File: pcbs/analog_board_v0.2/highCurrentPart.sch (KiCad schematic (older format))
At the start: 29 parts, among them P2 CONN_01X03, P3 CONN_01X03, Q1 MMBT3904, U1 AD8616

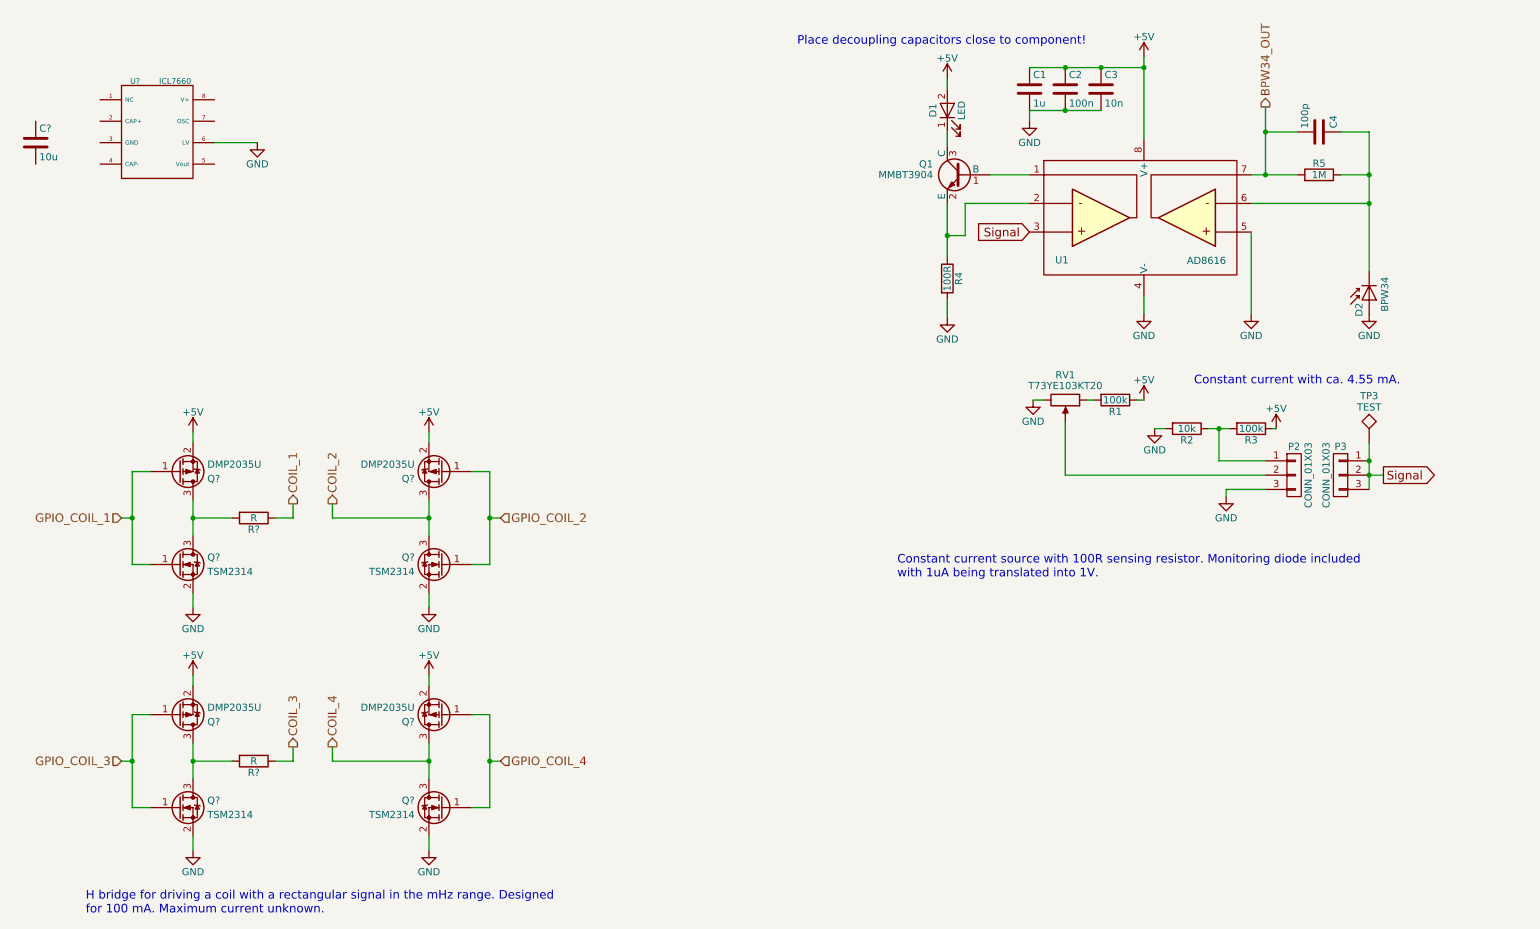
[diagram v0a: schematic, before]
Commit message: Finished schematics of the analog_board_v0.2 today.
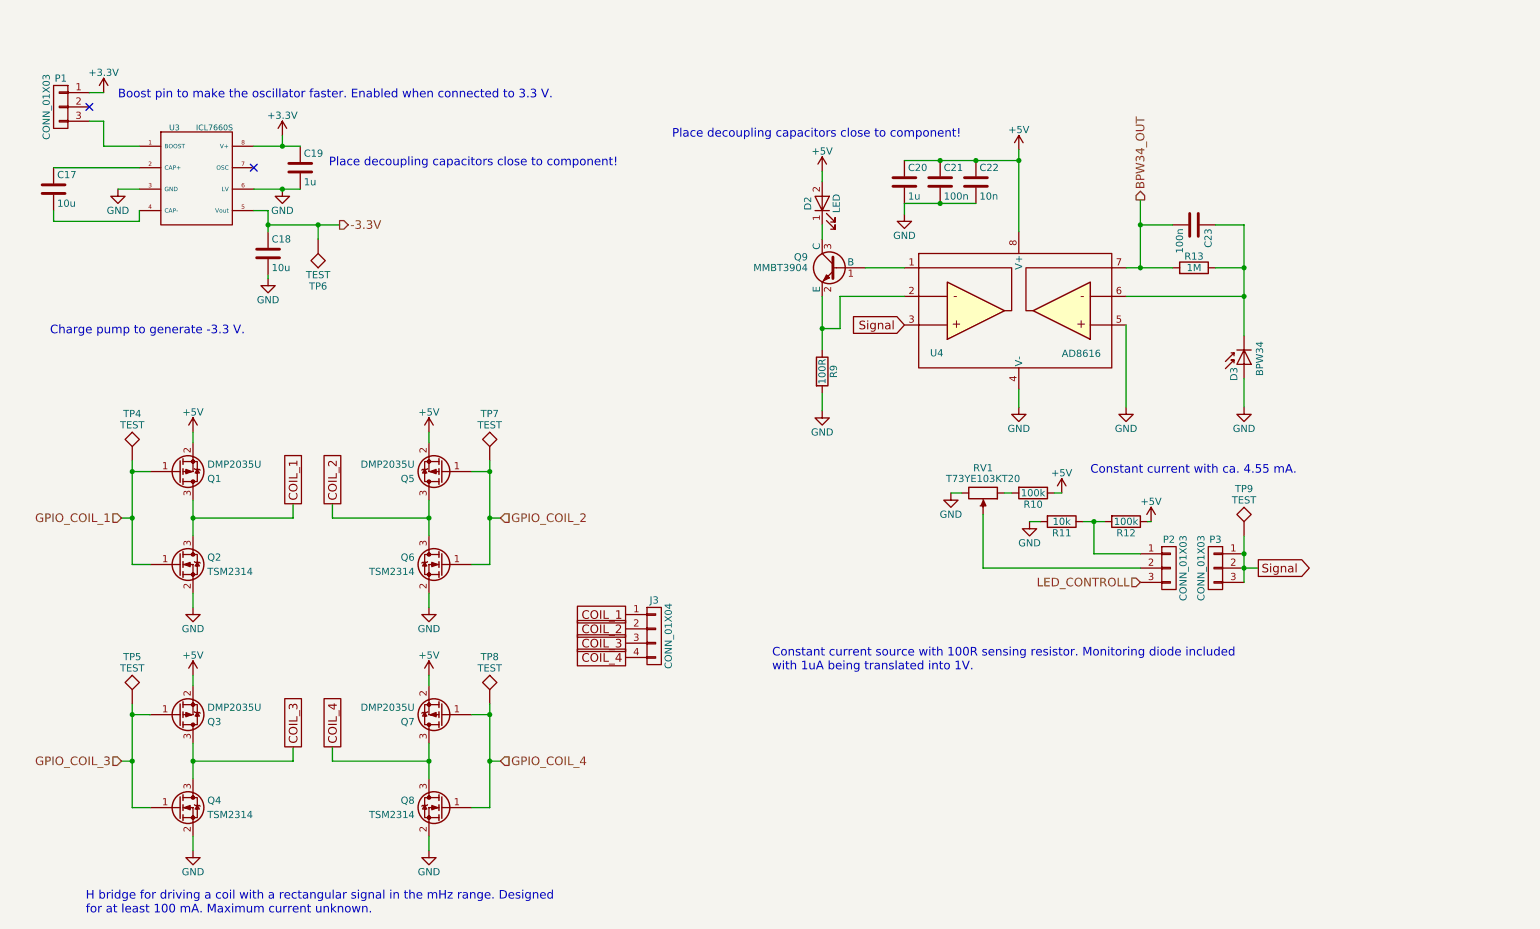
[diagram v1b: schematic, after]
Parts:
- removed C4: 100p, Resistors_SMD:R_0805, symbol C
- removed R? (x2): R, symbol R
- removed U?: ICL7660, SMD_Packages:SOIC-8-N, symbol ICL7660
- added C18: 10u, Resistors_SMD:R_0805, symbol C
- added C19: 1u, Resistors_SMD:R_0805, symbol C
- added C23: 100n, Resistors_SMD:R_0805, symbol C
- added J3: CONN_01X04, China Connectors:LED_CONN_1.25_PITCH, symbol CONN_01X04
- added P1: CONN_01X03, Samtec Connectors:Samtec-PHT-1-3-01-L-S, symbol CONN_01X03
- added TP4, TP5, TP6, TP7, TP8: TEST, Tespoints:TP_SMD_quadr_1mm, symbol TEST
- added U3: ICL7660S, SMD_Packages:SOIC-8-N, symbol ICL7660S
- C17: renamed from C?; Farnell 2496998 -> 1833812
- D2: renamed from D1; footprint LEDs:LED-5MM -> LEDs:LED_D5.0mm
- TP9: renamed from TP3; footprint Testpoints:TP_SMD_quadr_3mm -> Tespoints:TP_SMD_quadr_1mm
- gave numbers to parts that had none: 8
- renumbered C1 to C20, C2 to C21, C3 to C22, D2 to D3, Q1 to Q9, R1 to R10, R2 to R11, R3 to R12, R5 to R13, R4 to R9, U1 to U4
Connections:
- net BPW34_OUT: now also C23.2
- net COIL_1: now also Q1.3 (D), Q2.3 (D), J3.1 (P1)
- net COIL_2: now also J3.2 (P2)
- net COIL_3: now also Q3.3 (D), Q4.3 (D), J3.3 (P3)
- net COIL_4: now also J3.4 (P4)
- net GND: now also C18.2, C19.2, U3.3 (GND), U3.6 (LV); no longer P2.3 (P3)
- net GPIO_COIL_1: now also TP4.1
- net GPIO_COIL_2: now also TP7.1
- net GPIO_COIL_3: now also TP5.1
- net GPIO_COIL_4: now also TP8.1
- net at D3.1 (K), R13.1, U4.6: now also C23.1
- net at C17.1: now also U3.2 (CAP+)
- net at C17.2: now also U3.4 (CAP-)
- new net: P1.3 (P3), U3.1 (BOOST)
- new net +3V3: C19.1, P1.1 (P1), U3.8 (V+)
- new net -3.3V: C18.1, TP6.1, U3.5 (Vout)
- new net LED_CONTROLL: P2.3 (P3)
- no-connect marks 0 -> 2
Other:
- note added: "Boost pin to make the oscillator faster. Enabled when connected to 3.3 V."
- note added: "Charge pump to generate -3.3 V."
- note added: "H bridge for driving a coil with a rectangular signal in the mHz range. Designed\nfor at least 100 mA. Maximum current unknown."
- note removed: "H bridge for driving a coil with a rectangular signal in the mHz range. Designed\nfor 100 mA. Maximum current unknown."
- moved on the sheet: C17, C20, C21, C22, D2, D3, P2, P3, Q9, R10, R11, R12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

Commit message: Analog board basically finished.
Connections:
- net at P1.2 (P2): now also U3.1 (BOOST)
- net at P1.3 (P3): no longer U3.1 (BOOST)
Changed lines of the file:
@@
 $EndDescr
 $Comp
-L GND #PWR017
+L GND #PWR36
 U 1 1 5940A4E3
 P 8150 3325
-F 0 "#PWR017" H 8150 3075 50  0001 C CNN
+F 0 "#PWR36" H 8150 3075 50  0001 C CNN
 F 1 "GND" H 8150 3175 50  0000 C CNN
 F 2 "" H 8150 3325 50  0000 C CNN
@@
 $EndComp
 $Comp
-L GND #PWR018
+L GND #PWR41
 U 1 1 5940A554
 P 9725 3325
-F 0 "#PWR018" H 9725 3075 50  0001 C CNN
+F 0 "#PWR41" H 9725 3075 50  0001 C CNN
 F 1 "GND" H 9725 3175 50  0000 C CNN
 F 2 "" H 9725 3325 50  0000 C CNN
@@
 	6775 2050 6775 2150
 $Comp
-L +5V #PWR019
+L +5V #PWR31
 U 1 1 5940A5DC
 P 6775 1675
-F 0 "#PWR019" H 6775 1525 50  0001 C CNN
+F 0 "#PWR31" H 6775 1525 50  0001 C CNN
 F 1 "+5V" H 6775 1815 50  0000 C CNN
 F 2 "" H 6775 1675 50  0000 C CNN
@@
 	6775 1675 6775 1750
 $Comp
-L GND #PWR020
+L GND #PWR32
 U 1 1 5940A5E4
 P 6775 3350
-F 0 "#PWR020" H 6775 3100 50  0001 C CNN
+F 0 "#PWR32" H 6775 3100 50  0001 C CNN
 F 1 "GND" H 6775 3200 50  0000 C CNN
 F 2 "" H 6775 3350 50  0000 C CNN
@@
 Signal
 $Comp
-L GND #PWR021
+L GND #PWR34
 U 1 1 5940A601
 P 7675 3925
-F 0 "#PWR021" H 7675 3675 50  0001 C CNN
+F 0 "#PWR34" H 7675 3675 50  0001 C CNN
 F 1 "GND" H 7675 3775 50  0000 C CNN
 F 2 "" H 7675 3925 50  0000 C CNN
@@
 Signal
 $Comp
-L +5V #PWR022
+L +5V #PWR38
 U 1 1 5940A60A
 P 8450 3925
-F 0 "#PWR022" H 8450 3775 50  0001 C CNN
+F 0 "#PWR38" H 8450 3775 50  0001 C CNN
 F 1 "+5V" H 8450 4065 50  0000 C CNN
 F 2 "" H 8450 3925 50  0000 C CNN
@@
 Connection ~ 6775 2775
 $Comp
-L GND #PWR023
+L GND #PWR39
 U 1 1 5940EF10
 P 8900 3325
-F 0 "#PWR023" H 8900 3075 50  0001 C CNN
+F 0 "#PWR39" H 8900 3075 50  0001 C CNN
 F 1 "GND" H 8900 3175 50  0000 C CNN
 F 2 "" H 8900 3325 50  0000 C CNN
@@
 	8900 2750 8900 3325
 $Comp
-L +5V #PWR024
+L +5V #PWR35
 U 1 1 594122D1
 P 8150 1525
-F 0 "#PWR024" H 8150 1375 50  0001 C CNN
+F 0 "#PWR35" H 8150 1375 50  0001 C CNN
 F 1 "+5V" H 8150 1665 50  0000 C CNN
 F 2 "" H 8150 1525 50  0000 C CNN
@@
 Connection ~ 7600 1600
 $Comp
-L GND #PWR025
+L GND #PWR33
 U 1 1 594122F3
 P 7350 1975
-F 0 "#PWR025" H 7350 1725 50  0001 C CNN
+F 0 "#PWR33" H 7350 1725 50  0001 C CNN
 F 1 "GND" H 7350 1825 50  0000 C CNN
 F 2 "" H 7350 1975 50  0000 C CNN
@@
 $EndComp
 $Comp
-L +5V #PWR026
+L +5V #PWR40
 U 1 1 5941842E
 P 9075 4125
-F 0 "#PWR026" H 9075 3975 50  0001 C CNN
+F 0 "#PWR40" H 9075 3975 50  0001 C CNN
 F 1 "+5V" H 9075 4265 50  0000 C CNN
 F 2 "" H 9075 4125 50  0000 C CNN
@@
 	8600 4125 8750 4125
 $Comp
-L GND #PWR027
+L GND #PWR37
 U 1 1 5941869D
 P 8225 4125
-F 0 "#PWR027" H 8225 3875 50  0001 C CNN
+F 0 "#PWR37" H 8225 3875 50  0001 C CNN
 F 1 "GND" H 8225 3975 50  0000 C CNN
 F 2 "" H 8225 4125 50  0000 C CNN
@@
 BPW34_OUT
 $Comp
-L GND #PWR028
+L GND #PWR26
 U 1 1 59553CC6
 P 3000 1800
-F 0 "#PWR028" H 3000 1550 50  0001 C CNN
+F 0 "#PWR26" H 3000 1550 50  0001 C CNN
 F 1 "GND" H 3000 1650 50  0000 C CNN
 F 2 "" H 3000 1800 50  0001 C CNN
@@
 	2375 5675 2375 5925
 $Comp
-L GND #PWR029
+L GND #PWR23
 U 1 1 59557860
 P 2375 6425
-F 0 "#PWR029" H 2375 6175 50  0001 C CNN
+F 0 "#PWR23" H 2375 6175 50  0001 C CNN
 F 1 "GND" H 2375 6275 50  0000 C CNN
 F 2 "" H 2375 6425 50  0000 C CNN
@@
 	2375 6325 2375 6425
 $Comp
-L +5V #PWR030
+L +5V #PWR22
 U 1 1 59557DF9
 P 2375 5200
-F 0 "#PWR030" H 2375 5050 50  0001 C CNN
+F 0 "#PWR22" H 2375 5050 50  0001 C CNN
 F 1 "+5V" H 2375 5340 50  0000 C CNN
 F 2 "" H 2375 5200 50  0000 C CNN
@@
 	4025 5675 4025 5925
 $Comp
-L GND #PWR031
+L GND #PWR30
 U 1 1 59558304
 P 4025 6425
-F 0 "#PWR031" H 4025 6175 50  0001 C CNN
+F 0 "#PWR30" H 4025 6175 50  0001 C CNN
 F 1 "GND" H 4025 6275 50  0000 C CNN
 F 2 "" H 4025 6425 50  0000 C CNN
@@
 	4025 6325 4025 6425
 $Comp
-L +5V #PWR032
+L +5V #PWR29
 U 1 1 5955830B
 P 4025 5200
-F 0 "#PWR032" H 4025 5050 50  0001 C CNN
+F 0 "#PWR29" H 4025 5050 50  0001 C CNN
 F 1 "+5V" H 4025 5340 50  0000 C CNN
 F 2 "" H 4025 5200 50  0000 C CNN
@@
 	2375 3975 2375 4225
 $Comp
-L GND #PWR033
+L GND #PWR21
 U 1 1 5956291A
 P 2375 4725
-F 0 "#PWR033" H 2375 4475 50  0001 C CNN
+F 0 "#PWR21" H 2375 4475 50  0001 C CNN
 F 1 "GND" H 2375 4575 50  0000 C CNN
 F 2 "" H 2375 4725 50  0000 C CNN
@@
 	2375 4625 2375 4725
 $Comp
-L +5V #PWR034
+L +5V #PWR20
 U 1 1 59562921
 P 2375 3500
-F 0 "#PWR034" H 2375 3350 50  0001 C CNN
+F 0 "#PWR20" H 2375 3350 50  0001 C CNN
 F 1 "+5V" H 2375 3640 50  0000 C CNN
 F 2 "" H 2375 3500 50  0000 C CNN
@@
 	4025 3975 4025 4225
 $Comp
-L GND #PWR035
+L GND #PWR28
 U 1 1 59562931
 P 4025 4725
-F 0 "#PWR035" H 4025 4475 50  0001 C CNN
+F 0 "#PWR28" H 4025 4475 50  0001 C CNN
 F 1 "GND" H 4025 4575 50  0000 C CNN
 F 2 "" H 4025 4725 50  0000 C CNN
@@
 	4025 4625 4025 4725
 $Comp
-L +5V #PWR036
+L +5V #PWR27
 U 1 1 59562938
 P 4025 3500
-F 0 "#PWR036" H 4025 3350 50  0001 C CNN
+F 0 "#PWR27" H 4025 3350 50  0001 C CNN
 F 1 "+5V" H 4025 3640 50  0000 C CNN
 F 2 "" H 4025 3500 50  0000 C CNN
@@
 LED_CONTROLL
 $Comp
-L GND #PWR037
+L GND #PWR19
 U 1 1 59563916
 P 1850 1800
-F 0 "#PWR037" H 1850 1550 50  0001 C CNN
+F 0 "#PWR19" H 1850 1550 50  0001 C CNN
 F 1 "GND" H 1850 1650 50  0000 C CNN
 F 2 "" H 1850 1800 50  0001 C CNN
@@
 	2000 2025 2000 1950
 $Comp
-L +3.3V #PWR038
+L +3.3V #PWR25
 U 1 1 59563EC0
 P 3000 1425
-F 0 "#PWR038" H 3000 1275 50  0001 C CNN
+F 0 "#PWR25" H 3000 1275 50  0001 C CNN
 F 1 "+3.3V" H 3000 1565 50  0000 C CNN
 F 2 "" H 3000 1425 50  0001 C CNN
@@
 	2900 1950 2900 2100
 $Comp
-L GND #PWR039
+L GND #PWR24
 U 1 1 5956469D
 P 2900 2425
-F 0 "#PWR039" H 2900 2175 50  0001 C CNN
+F 0 "#PWR24" H 2900 2175 50  0001 C CNN
 F 1 "GND" H 2900 2275 50  0000 C CNN
 F 2 "" H 2900 2425 50  0001 C CNN
@@
 $EndComp
 $Comp
-L +3.3V #PWR040
+L +3.3V #PWR18
 U 1 1 595680C2
-P 1750 1125
-F 0 "#PWR040" H 1750 975 50  0001 C CNN
-F 1 "+3.3V" H 1750 1265 50  0000 C CNN
-F 2 "" H 1750 1125 50  0001 C CNN
-F 3 "" H 1750 1125 50  0001 C CNN
-	1    1750 1125
-	-1   0    0    -1
-$EndComp
-Wire Wire Line
-	1750 1125 1650 1125
-Wire Wire Line
-	1650 1325 1750 1325
-Wire Wire Line
-	1750 1325 1750 1500
-Wire Wire Line
-	1750 1500 2000 1500
-NoConn ~ 1650 1225
+P 1825 1125
+F 0 "#PWR18" H 1825 975 50  0001 C CNN
+F 1 "+3.3V" H 1825 1265 50  0000 C CNN
+F 2 "" H 1825 1125 50  0001 C CNN
+F 3 "" H 1825 1125 50  0001 C CNN
+	1    1825 1125
+	-1   0    0    -1
+$EndComp
+Wire Wire Line
+	1825 1125 1650 1125
+NoConn ~ 1650 1325
 Text Notes 1850 1175 0    60   ~ 0
 Boost pin to make the oscillator faster. Enabled when connected to 3.3 V.
@@
 	0    1    1    0
 $EndComp
+Wire Wire Line
+	1650 1225 1825 1225
+Wire Wire Line
+	1825 1225 1825 1500
+Wire Wire Line
+	1825 1500 2000 1500
 $EndSCHEMATC
